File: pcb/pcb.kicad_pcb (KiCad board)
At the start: 2 copper layers, 157.6 x 110.6 mm, 33 parts, among them J1 Conn_01x10, J2 Conn_01x06, J3 Conn_01x06, J4 Conn_01x06, J5 Conn_01x06, J6 Conn_01x06, J7 Conn_01x06, J8 Conn_01x10, U1 teensy-2.0

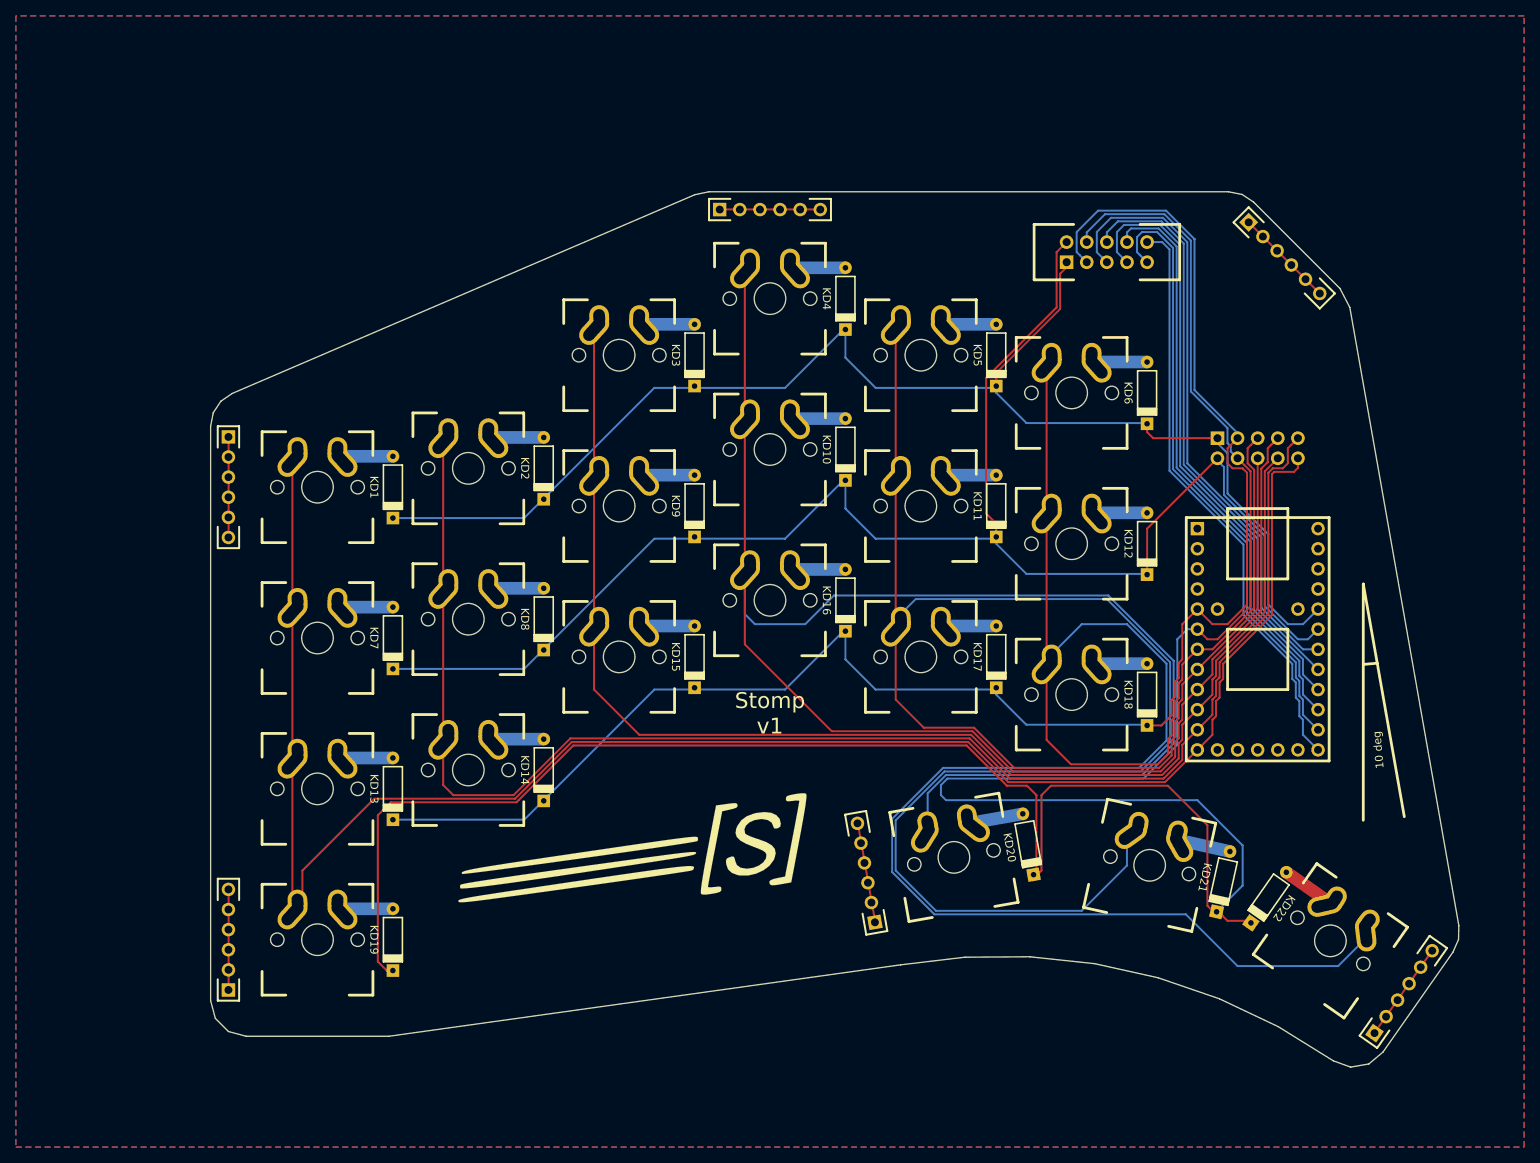
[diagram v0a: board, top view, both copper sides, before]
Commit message: Change board outline
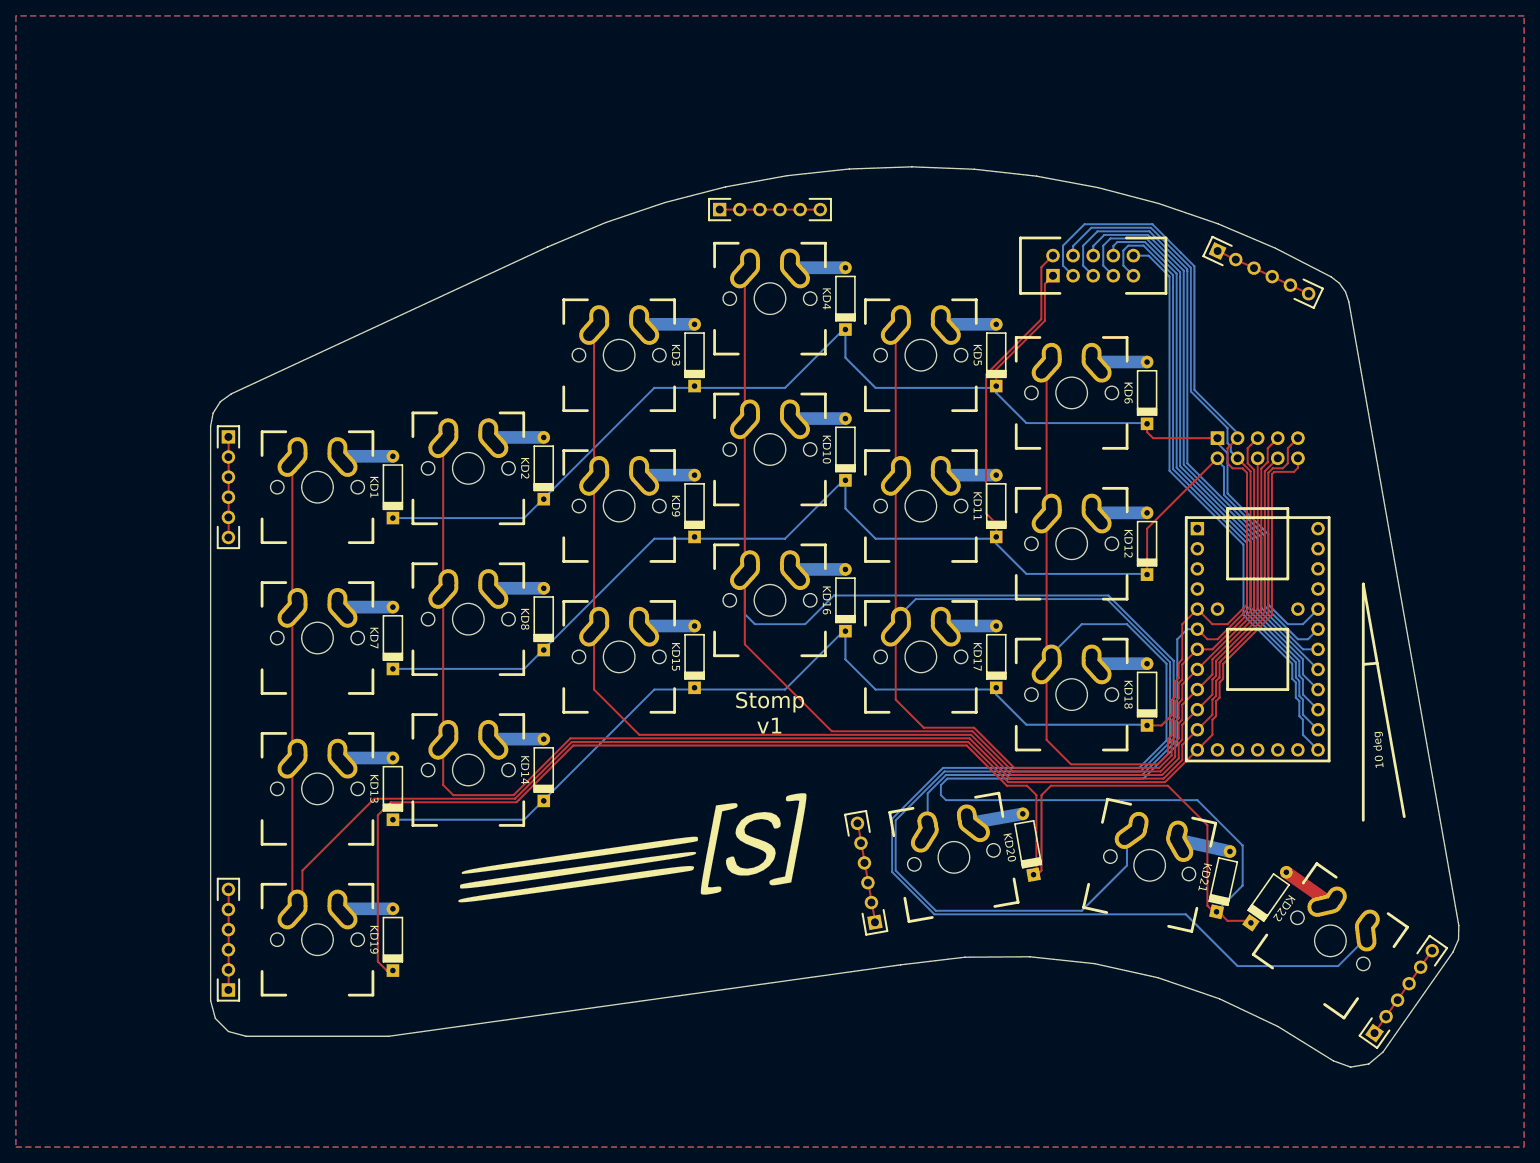
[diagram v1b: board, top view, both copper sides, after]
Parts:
- moved J7 5.34 mm to (8.90, -65.5), turned to 64.9 degrees
- moved J1 2.43 mm to (-6.80, -63.7)
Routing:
- net /R0: track 175.1 -> 172.6 mm
- net /R1: track 203.3 -> 200.9 mm
- net /R3: track 344.8 -> 343.7 mm
- net Net-(J1-Pad8): track 74.5 -> 73.5 mm
- net /R2: track 212.3 -> 211.3 mm
- net Net-(J1-Pad7): track 77.1 -> 76.1 mm
- net Net-(J1-Pad10): track 74.2 -> 73.2 mm
- net Net-(J1-Pad6): track 73.5 -> 72.5 mm
- net Net-(J1-Pad5): track 77.2 -> 76.2 mm
- net Net-(J1-Pad9): track 77.8 -> 77.0 mm
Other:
- board size 157.6 x 110.6 mm -> 157.6 x 113.7 mm

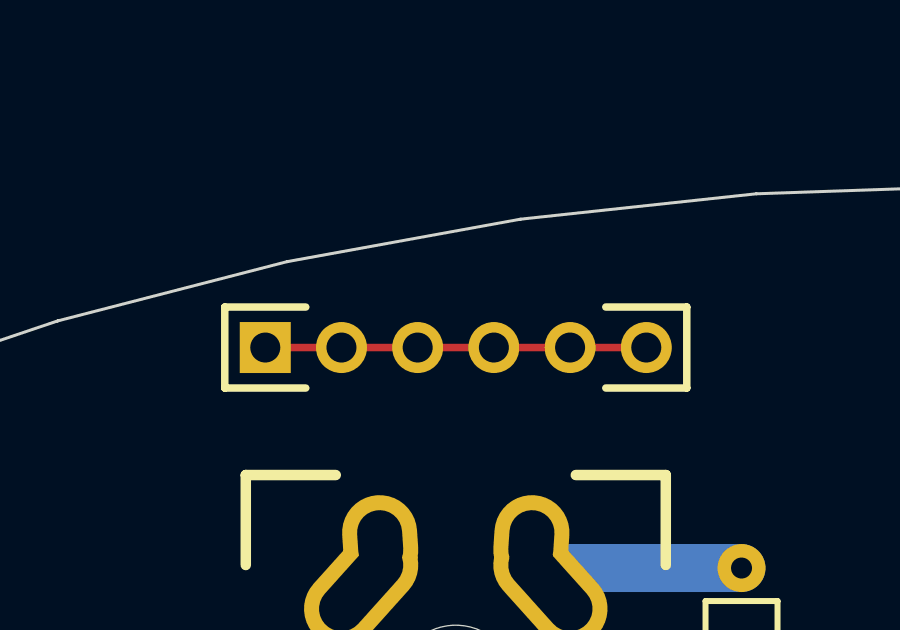
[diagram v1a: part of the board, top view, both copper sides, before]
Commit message: Fix one header
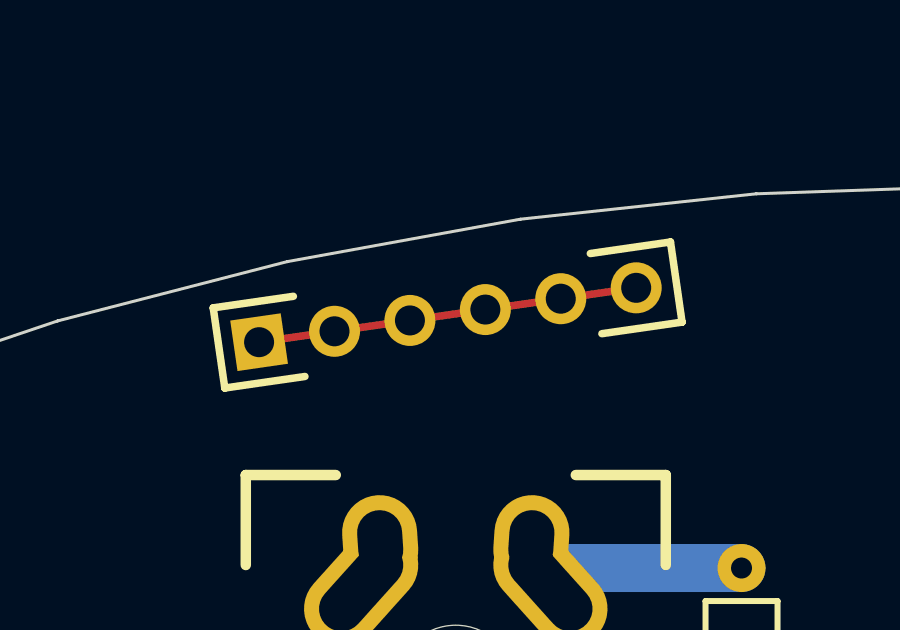
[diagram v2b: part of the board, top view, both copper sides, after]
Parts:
- moved J2 0.27 mm to (-54.2, -71.0), turned to 98.2 degrees
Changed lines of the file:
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@@
   )
   (module keyboard-parts:header_1x06_2.54mm (layer F.Cu)
-    (at -53.975 -70.78125 90)
-    (fp_text reference J2 (at 0 -2.33 90) (layer F.SilkS) hide
-      (effects (font (size 1 1) (thickness 0.15)))
-    )
-    (fp_text value Conn_01x06 (at 0 15.24 90) (layer F.Fab)
-      (effects (font (size 1 1) (thickness 0.15)))
-    )
-    (fp_text user %R (at 0 -2.33 90) (layer B.SilkS) hide
+    (at -54.181351 -70.959997 98.2)
+    (fp_text reference J2 (at 0 -2.33 98.2) (layer F.SilkS) hide
+      (effects (font (size 1 1) (thickness 0.15)))
+    )
+    (fp_text value Conn_01x06 (at 0 15.24 98.2) (layer F.Fab)
+      (effects (font (size 1 1) (thickness 0.15)))
+    )
+    (fp_text user %R (at 0 -2.33 98.2) (layer B.SilkS) hide
       (effects (font (size 1 1) (thickness 0.15)) (justify mirror))
     )
@@
     (fp_line (start 1.35 14.05) (end 1.35 11.35) (layer B.SilkS) (width 0.25))
     (fp_line (start -1.35 14.05) (end -1.35 11.35) (layer B.SilkS) (width 0.25))
-    (fp_text user %R (at 0 5.08) (layer F.Fab)
+    (fp_text user %R (at 0 5.08 8.2) (layer F.Fab)
       (effects (font (size 1 1) (thickness 0.15)))
     )
@@
     (fp_line (start -1.35 14.05) (end -1.35 11.35) (layer F.SilkS) (width 0.25))
     (fp_line (start -1.35 -1.35) (end 1.35 -1.35) (layer F.SilkS) (width 0.25))
-    (pad 6 thru_hole oval (at 0 12.7 90) (size 1.7 1.7) (drill 1) (layers *.Cu *.Mask)
-      (net 5 "Net-(J2-Pad1)"))
-    (pad 4 thru_hole oval (at 0 7.62 90) (size 1.7 1.7) (drill 1) (layers *.Cu *.Mask)
-      (net 5 "Net-(J2-Pad1)"))
-    (pad 3 thru_hole oval (at 0 5.08 90) (size 1.7 1.7) (drill 1) (layers *.Cu *.Mask)
-      (net 5 "Net-(J2-Pad1)"))
-    (pad 2 thru_hole oval (at 0 2.54 90) (size 1.7 1.7) (drill 1) (layers *.Cu *.Mask)
-      (net 5 "Net-(J2-Pad1)"))
-    (pad 1 thru_hole rect (at 0 0 90) (size 1.7 1.7) (drill 1) (layers *.Cu *.Mask)
-      (net 5 "Net-(J2-Pad1)"))
-    (pad 5 thru_hole oval (at 0 10.16 90) (size 1.7 1.7) (drill 1) (layers *.Cu *.Mask)
+    (pad 6 thru_hole oval (at 0 12.7 98.2) (size 1.7 1.7) (drill 1) (layers *.Cu *.Mask)
+      (net 5 "Net-(J2-Pad1)"))
+    (pad 4 thru_hole oval (at 0 7.62 98.2) (size 1.7 1.7) (drill 1) (layers *.Cu *.Mask)
+      (net 5 "Net-(J2-Pad1)"))
+    (pad 3 thru_hole oval (at 0 5.08 98.2) (size 1.7 1.7) (drill 1) (layers *.Cu *.Mask)
+      (net 5 "Net-(J2-Pad1)"))
+    (pad 2 thru_hole oval (at 0 2.54 98.2) (size 1.7 1.7) (drill 1) (layers *.Cu *.Mask)
+      (net 5 "Net-(J2-Pad1)"))
+    (pad 1 thru_hole rect (at 0 0 98.2) (size 1.7 1.7) (drill 1) (layers *.Cu *.Mask)
+      (net 5 "Net-(J2-Pad1)"))
+    (pad 5 thru_hole oval (at 0 10.16 98.2) (size 1.7 1.7) (drill 1) (layers *.Cu *.Mask)
       (net 5 "Net-(J2-Pad1)"))
     (model ${KISYS3DMOD}/Connector_PinHeader_2.54mm.3dshapes/PinHeader_1x06_P2.54mm_Vertical.wrl
@@
   (segment (start -19.05 -48.487501) (end -19.05 -50.5968) (width 0.25) (layer F.Cu) (net 4))
   (segment (start -12.9032 -56.7436) (end -12.9032 -61.3918) (width 0.25) (layer F.Cu) (net 4))
-  (segment (start -53.975 -70.78125) (end -41.29185 -70.78125) (width 0.25) (layer F.Cu) (net 5))
+  (segment (start -54.181351 -70.959997) (end -41.627871 -72.768981) (width 0.25) (layer F.Cu) (net 5))
   (segment (start -116.025 -42.06875) (end -116.025 -42.025) (width 0.25) (layer F.Cu) (net 6))
   (segment (start -116.025 -42.025) (end -116 -42) (width 0.25) (layer F.Cu) (net 6))

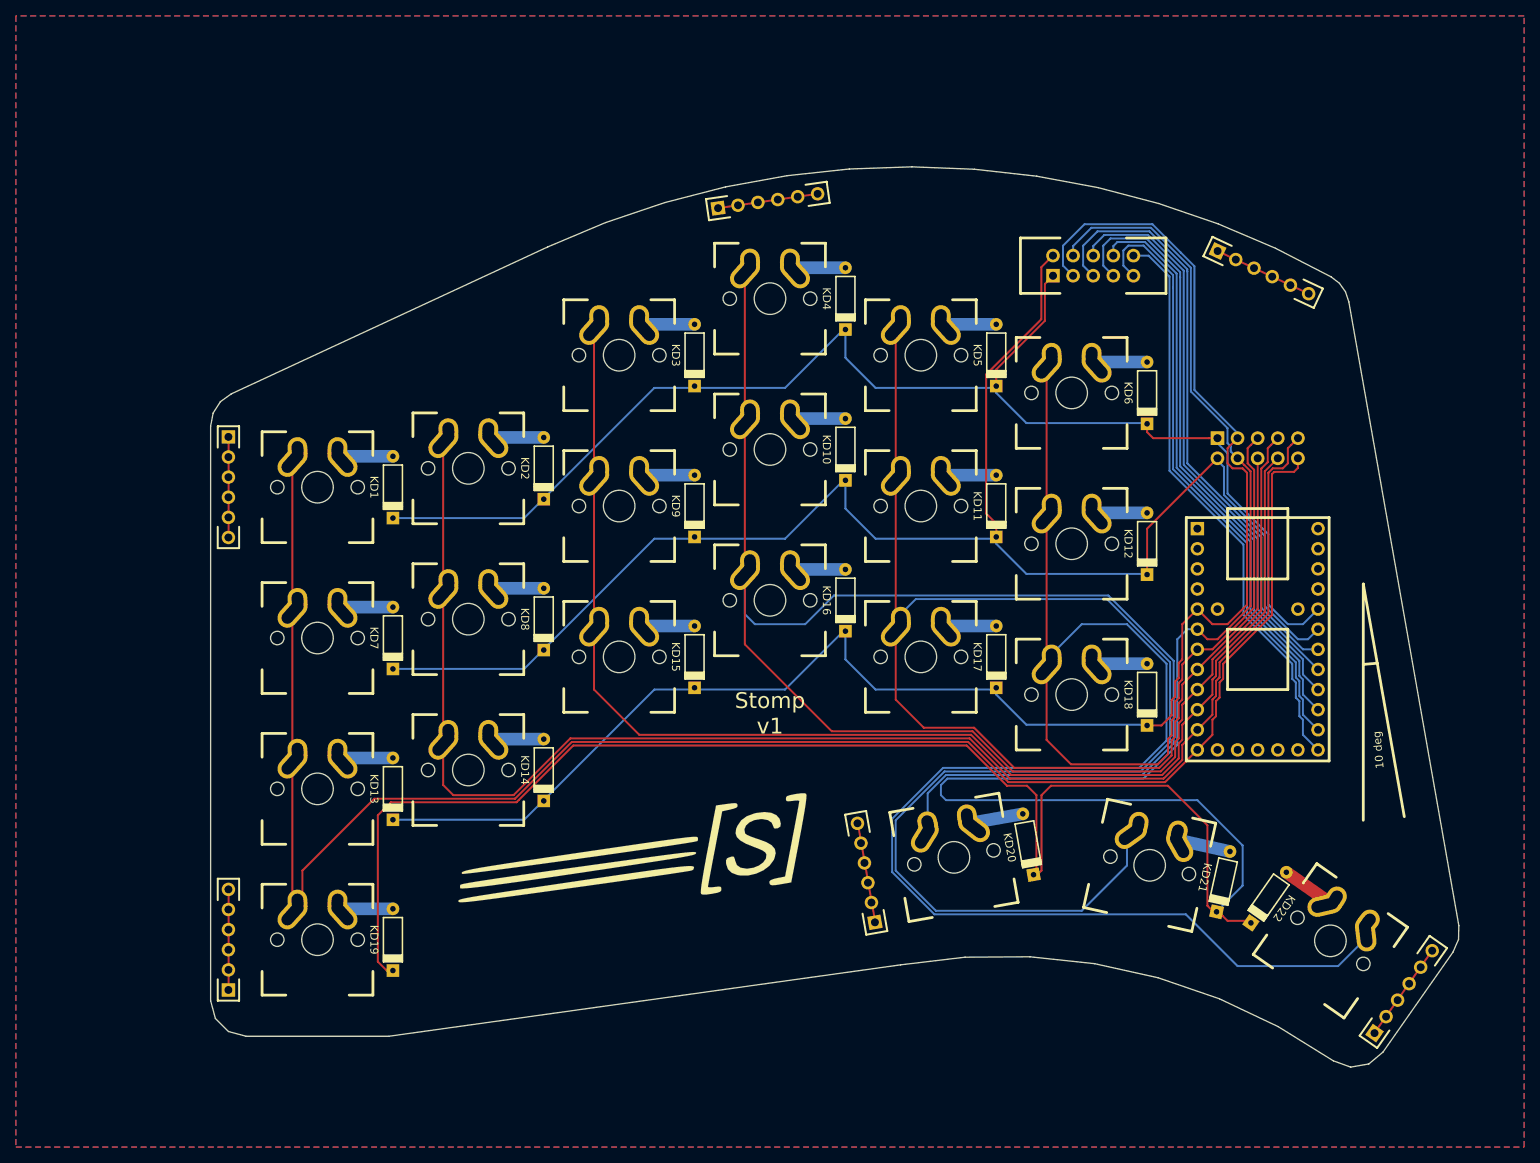
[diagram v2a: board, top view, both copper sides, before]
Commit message: Finish refinement of board outline
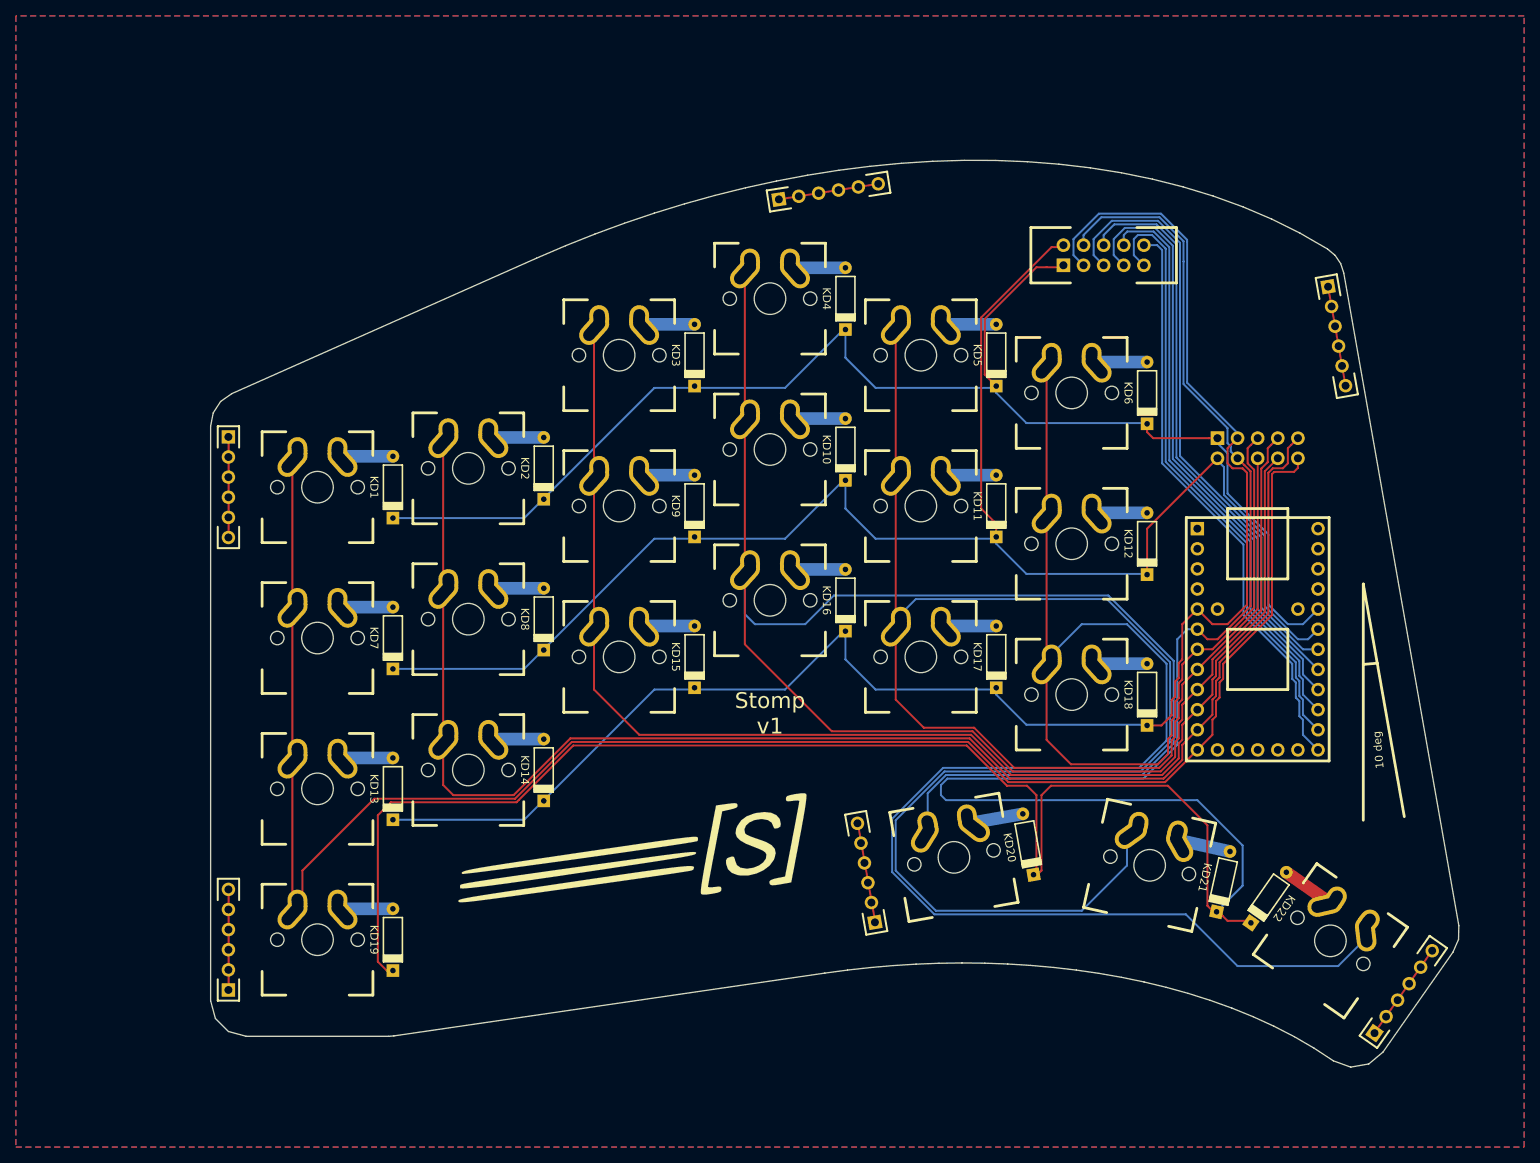
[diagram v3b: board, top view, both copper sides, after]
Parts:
- moved J7 14.7 mm to (22.9, -61.0), turned to 10 degrees
- moved J2 7.76 mm to (-46.5, -72.1), turned to 98.9 degrees
- moved J1 1.87 mm to (-5.48, -65.0)
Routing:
- net /R0: track 172.6 -> 177.2 mm
- net /R1: track 200.9 -> 203.7 mm
- net Net-(J1-Pad5): track 76.2 -> 77.0 mm
- net /R3: track 343.7 -> 344.5 mm
- net Net-(J1-Pad8): track 73.5 -> 74.2 mm
- net Net-(J1-Pad6): track 72.5 -> 73.2 mm
- net Net-(J1-Pad10): track 73.2 -> 73.8 mm
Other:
- board size 157.6 x 113.7 mm -> 157.6 x 114.5 mm

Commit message: Change pin for column B to avoid teensy LED
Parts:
- removed G***: LOGO, logos:smark-rev
- removed G***: LOGO, logos:smark
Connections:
- U1 pad 18: Net-(J1-Pad10) -> (no net)
- U1 pad 2: (no net) -> Net-(J1-Pad10)
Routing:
- net Net-(J1-Pad10): track 73.8 -> 43.7 mm

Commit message: Slight reposition and reroute of inter-pcb-header
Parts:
- added G***: LOGO, logos:smark-rev, F.Cu at (-64.8, 12.7)
- added G***: LOGO, logos:smark, B.Cu at (-64.8, 12.7)
- moved J8 0.89 mm to (14.0, -39.8)
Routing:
- net /R1: track 203.7 -> 201.7 mm
- net /C0-CB: track 227.9 -> 226.5 mm
- net /R3: track 344.5 -> 343.0 mm
- net /C5-C6: track 250.1 -> 249.2 mm
- net /C3-C8: track 266.2 -> 265.3 mm
- net /C4-C7: track 265.9 -> 265.0 mm
- net /C1-CA: track 189.4 -> 188.5 mm
- net /C2-C9: track 166.5 -> 165.6 mm
